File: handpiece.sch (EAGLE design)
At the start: 26 parts, among them IC1 MEGA8-P

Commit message: text marker besides con
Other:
- note added: "To Centerpiece"
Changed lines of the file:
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@@
 <text x="96.52" y="-2.54" size="1.778" layer="97">Only populated on Left-Handpiece</text>
 <text x="5.08" y="-2.54" size="1.778" layer="97">Only populated on Right-Handpiece</text>
+<text x="154.94" y="96.52" size="1.778" layer="97">To Centerpiece</text>
 </plain>
 <instances>

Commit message: proof of concept routing
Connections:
- net D: now also IC1.PB1(OC1A); no longer IC1.PB2(SS/OC1B)
- net EA: now also IC1.PD2(INT0); no longer IC1.PD3(INT1)
- net KR: now also IC1.PD0(RXD); no longer IC1.PD1(TXD)
- net N: now also IC1.PB0(ICP); no longer IC1.PD2(INT0)
- net OU: now also IC1.PD3(INT1); no longer IC1.PD4(XCK/T0)
- net SS: now also IC1.PD1(TXD); no longer IC1.PD0(RXD)
- net Z: now also IC1.PB2(SS/OC1B); no longer IC1.PB1(OC1A)
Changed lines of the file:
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@@
 <setting verticaltext="up"/>
 </settings>
-<grid distance="0.1" unitdist="inch" unit="inch" style="lines" multiple="1" display="yes" altdistance="0.01" altunitdist="inch" altunit="inch"/>
+<grid distance="0.1" unitdist="inch" unit="inch" style="lines" multiple="1" display="no" altdistance="0.01" altunitdist="inch" altunit="inch"/>
 <layers>
 <layer number="1" name="Top" color="4" fill="1" visible="no" active="no"/>
@@
 </segment>
 <segment>
-<pinref part="IC1" gate="G$1" pin="PD0(RXD)"/>
-<wire x1="157.48" y1="10.16" x2="170.18" y2="10.16" width="0.1524" layer="91"/>
+<pinref part="IC1" gate="G$1" pin="PD1(TXD)"/>
+<wire x1="157.48" y1="12.7" x2="170.18" y2="12.7" width="0.1524" layer="91"/>
 </segment>
 </net>
@@
 </segment>
 <segment>
-<pinref part="IC1" gate="G$1" pin="PD1(TXD)"/>
-<wire x1="157.48" y1="12.7" x2="170.18" y2="12.7" width="0.1524" layer="91"/>
+<pinref part="IC1" gate="G$1" pin="PD0(RXD)"/>
+<wire x1="157.48" y1="10.16" x2="170.18" y2="10.16" width="0.1524" layer="91"/>
 </segment>
 </net>
@@
 </segment>
 <segment>
-<pinref part="IC1" gate="G$1" pin="PB1(OC1A)"/>
-<wire x1="157.48" y1="35.56" x2="170.18" y2="35.56" width="0.1524" layer="91"/>
+<pinref part="IC1" gate="G$1" pin="PB2(SS/OC1B)"/>
+<wire x1="157.48" y1="38.1" x2="170.18" y2="38.1" width="0.1524" layer="91"/>
 </segment>
 </net>
@@
 <pinref part="E" gate="G$1" pin="PIN-2"/>
 <wire x1="5.08" y1="-22.86" x2="5.08" y2="-12.7" width="0.1524" layer="91"/>
+<wire x1="5.08" y1="-12.7" x2="53.34" y2="-12.7" width="0.1524" layer="91"/>
+<wire x1="53.34" y1="-12.7" x2="53.34" y2="2.54" width="0.1524" layer="91"/>
 <pinref part="A" gate="G$1" pin="PIN-2"/>
-<wire x1="5.08" y1="-12.7" x2="53.34" y2="-12.7" width="0.1524" layer="91"/>
 <wire x1="53.34" y1="-12.7" x2="99.06" y2="-12.7" width="0.1524" layer="91"/>
 <wire x1="99.06" y1="-12.7" x2="99.06" y2="-22.86" width="0.1524" layer="91"/>
-<wire x1="53.34" y1="-12.7" x2="53.34" y2="2.54" width="0.1524" layer="91"/>
-<junction x="53.34" y="-12.7"/>
+</segment>
+<segment>
+<pinref part="IC1" gate="G$1" pin="PD2(INT0)"/>
+<wire x1="157.48" y1="15.24" x2="170.18" y2="15.24" width="0.1524" layer="91"/>
+</segment>
+</net>
+<net name="OU" class="0">
+<segment>
+<pinref part="U" gate="G$1" pin="PIN-2"/>
+<wire x1="30.48" y1="-22.86" x2="30.48" y2="-15.24" width="0.1524" layer="91"/>
+<wire x1="30.48" y1="-15.24" x2="55.88" y2="-15.24" width="0.1524" layer="91"/>
+<wire x1="55.88" y1="-15.24" x2="121.92" y2="-15.24" width="0.1524" layer="91"/>
+<wire x1="55.88" y1="2.54" x2="55.88" y2="-15.24" width="0.1524" layer="91"/>
+<junction x="55.88" y="-15.24"/>
+<pinref part="O" gate="G$1" pin="PIN-2"/>
+<wire x1="121.92" y1="-15.24" x2="121.92" y2="-22.86" width="0.1524" layer="91"/>
 </segment>
 <segment>
@@
 </segment>
 </net>
-<net name="OU" class="0">
-<segment>
-<pinref part="U" gate="G$1" pin="PIN-2"/>
-<wire x1="30.48" y1="-22.86" x2="30.48" y2="-15.24" width="0.1524" layer="91"/>
-<pinref part="O" gate="G$1" pin="PIN-2"/>
-<wire x1="30.48" y1="-15.24" x2="55.88" y2="-15.24" width="0.1524" layer="91"/>
-<wire x1="55.88" y1="-15.24" x2="121.92" y2="-15.24" width="0.1524" layer="91"/>
-<wire x1="121.92" y1="-15.24" x2="121.92" y2="-22.86" width="0.1524" layer="91"/>
-<wire x1="55.88" y1="2.54" x2="55.88" y2="-15.24" width="0.1524" layer="91"/>
-<junction x="55.88" y="-15.24"/>
-</segment>
-<segment>
-<pinref part="IC1" gate="G$1" pin="PD4(XCK/T0)"/>
-<wire x1="157.48" y1="20.32" x2="170.18" y2="20.32" width="0.1524" layer="91"/>
-</segment>
-</net>
 <net name="D" class="0">
-<segment>
-<pinref part="IC1" gate="G$1" pin="PB2(SS/OC1B)"/>
-<wire x1="157.48" y1="38.1" x2="170.18" y2="38.1" width="0.1524" layer="91"/>
-</segment>
 <segment>
 <pinref part="D" gate="G$1" pin="PIN-2"/>
 <wire x1="114.3" y1="48.26" x2="111.76" y2="48.26" width="0.1524" layer="91"/>
 <wire x1="111.76" y1="2.54" x2="111.76" y2="48.26" width="0.1524" layer="91"/>
+</segment>
+<segment>
+<pinref part="IC1" gate="G$1" pin="PB1(OC1A)"/>
+<wire x1="157.48" y1="35.56" x2="170.18" y2="35.56" width="0.1524" layer="91"/>
 </segment>
 </net>
@@
 </segment>
 <segment>
-<pinref part="IC1" gate="G$1" pin="PD2(INT0)"/>
-<wire x1="157.48" y1="15.24" x2="170.18" y2="15.24" width="0.1524" layer="91"/>
-</segment>
-</net>
+<pinref part="IC1" gate="G$1" pin="PB0(ICP)"/>
+<wire x1="157.48" y1="33.02" x2="170.18" y2="33.02" width="0.1524" layer="91"/>
+</segment>
+</net>

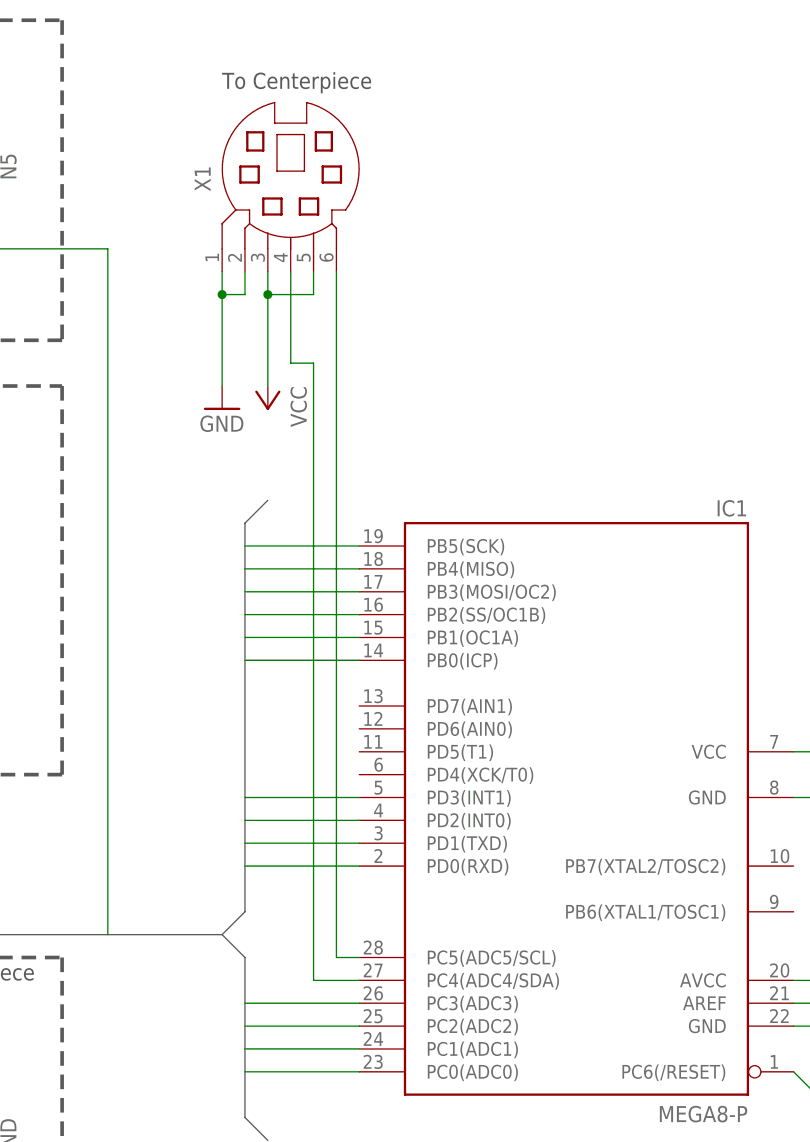
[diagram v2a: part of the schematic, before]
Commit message: add second connector (only one populated on one board)
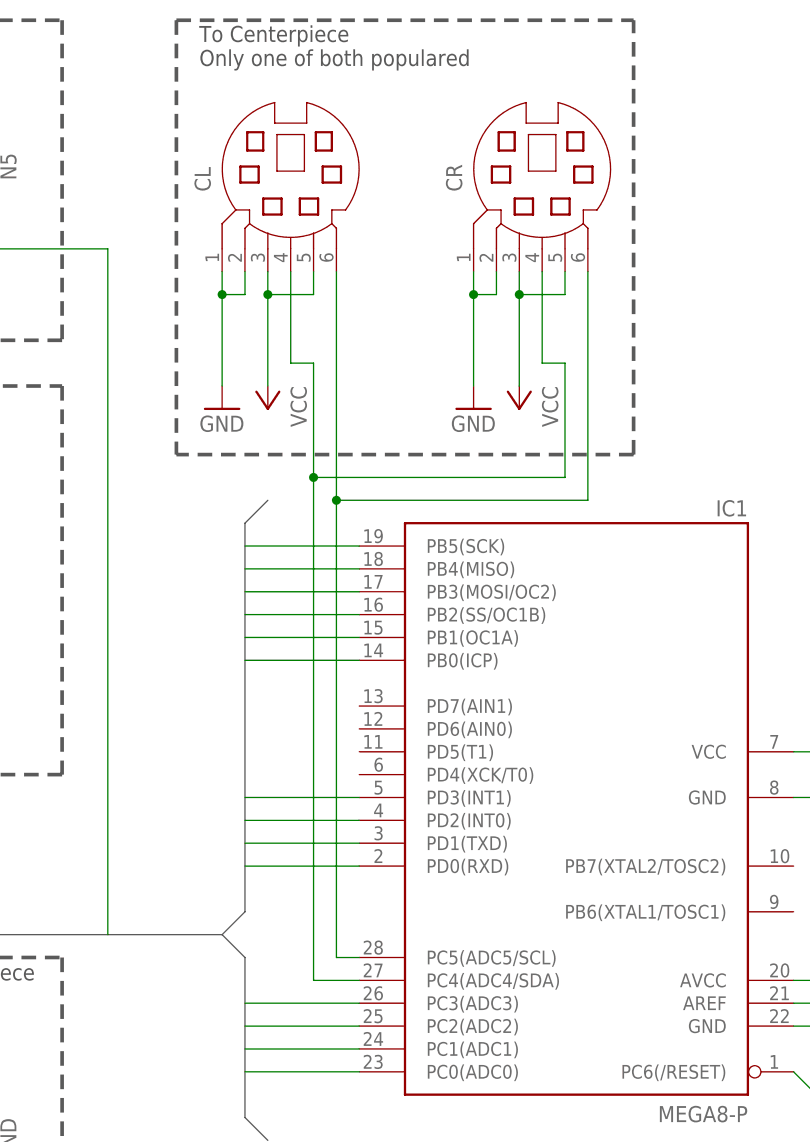
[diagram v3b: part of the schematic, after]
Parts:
- added CR: (no value), con-yamaichi:MD06SS
- renumbered X1 to CL
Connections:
- net GND: now also CR.1, CR.2
- net SCL: now also CR.6
- net SDA: now also CR.4
- net VCC: now also CR.3, CR.5
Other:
- note added: "To Centerpiece Only one of both populared"
- note removed: "To Centerpiece"
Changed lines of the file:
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@@
 <?xml version="1.0" encoding="utf-8"?>
 <!DOCTYPE eagle SYSTEM "eagle.dtd">
-<eagle version="6.4">
+<eagle version="6.5.0">
 <drawing>
 <settings>
@@
 <setting verticaltext="up"/>
 </settings>
-<grid distance="0.1" unitdist="inch" unit="inch" style="lines" multiple="1" display="no" altdistance="0.01" altunitdist="inch" altunit="inch"/>
+<grid distance="0.1" unitdist="inch" unit="inch" style="lines" multiple="1" display="yes" altdistance="0.01" altunitdist="inch" altunit="inch"/>
 <layers>
 <layer number="1" name="Top" color="4" fill="1" visible="no" active="no"/>
@@
 <part name="GND16" library="supply1" deviceset="GND" device=""/>
 <part name="GND17" library="supply1" deviceset="GND" device=""/>
-<part name="X1" library="con-yamaichi" deviceset="MD06SS" device=""/>
+<part name="CL" library="con-yamaichi" deviceset="MD06SS" device=""/>
 <part name="GND18" library="supply1" deviceset="GND" device=""/>
 <part name="P+6" library="supply1" deviceset="VCC" device=""/>
@@
 <part name="GND19" library="supply1" deviceset="GND" device=""/>
 <part name="GND20" library="supply1" deviceset="GND" device=""/>
+<part name="CR" library="con-yamaichi" deviceset="MD06SS" device=""/>
+<part name="GND21" library="supply1" deviceset="GND" device=""/>
+<part name="P+5" library="supply1" deviceset="VCC" device=""/>
 </parts>
 <sheets>
@@
 <text x="96.52" y="-2.54" size="1.778" layer="97">Only populated on Left-Handpiece</text>
 <text x="5.08" y="-2.54" size="1.778" layer="97">Only populated on Right-Handpiece</text>
-<text x="154.94" y="96.52" size="1.778" layer="97">To Centerpiece</text>
+<text x="152.4" y="99.06" size="1.778" layer="97">To Centerpiece
+Only one of both populared</text>
+<wire x1="149.86" y1="104.14" x2="200.66" y2="104.14" width="0.4064" layer="97" style="shortdash"/>
+<wire x1="200.66" y1="55.88" x2="200.66" y2="104.14" width="0.4064" layer="97" style="shortdash"/>
+<wire x1="200.66" y1="55.88" x2="149.86" y2="55.88" width="0.4064" layer="97" style="shortdash"/>
+<wire x1="149.86" y1="104.14" x2="149.86" y2="55.88" width="0.4064" layer="97" style="shortdash"/>
 </plain>
 <instances>
@@
 <instance part="GND16" gate="1" x="91.44" y="38.1" rot="R180"/>
 <instance part="GND17" gate="1" x="114.3" y="38.1" rot="R180"/>
-<instance part="X1" gate="G$1" x="162.56" y="86.36" rot="R90"/>
+<instance part="CL" gate="G$1" x="162.56" y="86.36" rot="R90"/>
 <instance part="GND18" gate="1" x="154.94" y="60.96"/>
 <instance part="P+6" gate="VCC" x="160.02" y="60.96" rot="R180"/>
@@
 <instance part="GND19" gate="1" x="106.68" y="-20.32" rot="R90"/>
 <instance part="GND20" gate="1" x="129.54" y="-20.32" rot="R90"/>
+<instance part="CR" gate="G$1" x="190.5" y="86.36" rot="R90"/>
+<instance part="GND21" gate="1" x="182.88" y="60.96"/>
+<instance part="P+5" gate="VCC" x="187.96" y="60.96" rot="R180"/>
 </instances>
 <busses>
@@
 <segment>
 <pinref part="GND18" gate="1" pin="GND"/>
-<pinref part="X1" gate="G$1" pin="1"/>
+<pinref part="CL" gate="G$1" pin="1"/>
 <wire x1="154.94" y1="63.5" x2="154.94" y2="73.66" width="0.1524" layer="91"/>
-<pinref part="X1" gate="G$1" pin="2"/>
+<pinref part="CL" gate="G$1" pin="2"/>
 <wire x1="154.94" y1="73.66" x2="154.94" y2="76.2" width="0.1524" layer="91"/>
 <wire x1="157.48" y1="76.2" x2="157.48" y2="73.66" width="0.1524" layer="91"/>
@@
 <wire x1="127" y1="-22.86" x2="127" y2="-20.32" width="0.1524" layer="91"/>
 </segment>
+<segment>
+<pinref part="GND21" gate="1" pin="GND"/>
+<pinref part="CR" gate="G$1" pin="1"/>
+<wire x1="182.88" y1="63.5" x2="182.88" y2="73.66" width="0.1524" layer="91"/>
+<pinref part="CR" gate="G$1" pin="2"/>
+<wire x1="182.88" y1="73.66" x2="182.88" y2="76.2" width="0.1524" layer="91"/>
+<wire x1="182.88" y1="73.66" x2="185.42" y2="73.66" width="0.1524" layer="91"/>
+<wire x1="185.42" y1="73.66" x2="185.42" y2="76.2" width="0.1524" layer="91"/>
+<junction x="182.88" y="73.66"/>
+</segment>
 </net>
 <net name="VCC" class="0">
@@
 </segment>
 <segment>
-<pinref part="X1" gate="G$1" pin="3"/>
+<pinref part="CL" gate="G$1" pin="3"/>
 <pinref part="P+6" gate="VCC" pin="VCC"/>
 <wire x1="160.02" y1="76.2" x2="160.02" y2="73.66" width="0.1524" layer="91"/>
-<pinref part="X1" gate="G$1" pin="5"/>
+<pinref part="CL" gate="G$1" pin="5"/>
 <wire x1="160.02" y1="73.66" x2="160.02" y2="63.5" width="0.1524" layer="91"/>
 <wire x1="165.1" y1="76.2" x2="165.1" y2="73.66" width="0.1524" layer="91"/>
 <wire x1="165.1" y1="73.66" x2="160.02" y2="73.66" width="0.1524" layer="91"/>
 <junction x="160.02" y="73.66"/>
+</segment>
+<segment>
+<pinref part="P+5" gate="VCC" pin="VCC"/>
+<pinref part="CR" gate="G$1" pin="3"/>
+<wire x1="187.96" y1="63.5" x2="187.96" y2="73.66" width="0.1524" layer="91"/>
+<pinref part="CR" gate="G$1" pin="5"/>
+<wire x1="187.96" y1="73.66" x2="187.96" y2="76.2" width="0.1524" layer="91"/>
+<wire x1="187.96" y1="73.66" x2="193.04" y2="73.66" width="0.1524" layer="91"/>
+<wire x1="193.04" y1="73.66" x2="193.04" y2="76.2" width="0.1524" layer="91"/>
+<junction x="187.96" y="73.66"/>
 </segment>
 </net>
@@
 <pinref part="IC1" gate="G$1" pin="PC5(ADC5/SCL)"/>
 <wire x1="170.18" y1="0" x2="167.64" y2="0" width="0.1524" layer="91"/>
-<wire x1="167.64" y1="0" x2="167.64" y2="76.2" width="0.1524" layer="91"/>
-<pinref part="X1" gate="G$1" pin="6"/>
+<wire x1="167.64" y1="0" x2="167.64" y2="50.8" width="0.1524" layer="91"/>
+<pinref part="CL" gate="G$1" pin="6"/>
+<pinref part="CR" gate="G$1" pin="6"/>
+<wire x1="167.64" y1="50.8" x2="167.64" y2="76.2" width="0.1524" layer="91"/>
+<wire x1="195.58" y1="76.2" x2="195.58" y2="50.8" width="0.1524" layer="91"/>
+<wire x1="195.58" y1="50.8" x2="167.64" y2="50.8" width="0.1524" layer="91"/>
+<junction x="167.64" y="50.8"/>
 </segment>
 </net>
@@
 <pinref part="IC1" gate="G$1" pin="PC4(ADC4/SDA)"/>
 <wire x1="170.18" y1="-2.54" x2="165.1" y2="-2.54" width="0.1524" layer="91"/>
-<wire x1="165.1" y1="-2.54" x2="165.1" y2="66.04" width="0.1524" layer="91"/>
-<pinref part="X1" gate="G$1" pin="4"/>
+<wire x1="165.1" y1="-2.54" x2="165.1" y2="53.34" width="0.1524" layer="91"/>
+<pinref part="CL" gate="G$1" pin="4"/>
+<wire x1="165.1" y1="53.34" x2="165.1" y2="66.04" width="0.1524" layer="91"/>
 <wire x1="162.56" y1="76.2" x2="162.56" y2="66.04" width="0.1524" layer="91"/>
 <wire x1="165.1" y1="66.04" x2="162.56" y2="66.04" width="0.1524" layer="91"/>
-</segment>
-</net>
+<pinref part="CR" gate="G$1" pin="4"/>
+<wire x1="190.5" y1="76.2" x2="190.5" y2="66.04" width="0.1524" layer="91"/>
+<wire x1="190.5" y1="66.04" x2="193.04" y2="66.04" width="0.1524" layer="91"/>
+<wire x1="193.04" y1="66.04" x2="193.04" y2="53.34" width="0.1524" layer="91"/>
+<wire x1="193.04" y1="53.34" x2="165.1" y2="53.34" width="0.1524" layer="91"/>
+<junction x="165.1" y="53.34"/>
+</segment>
+</net>

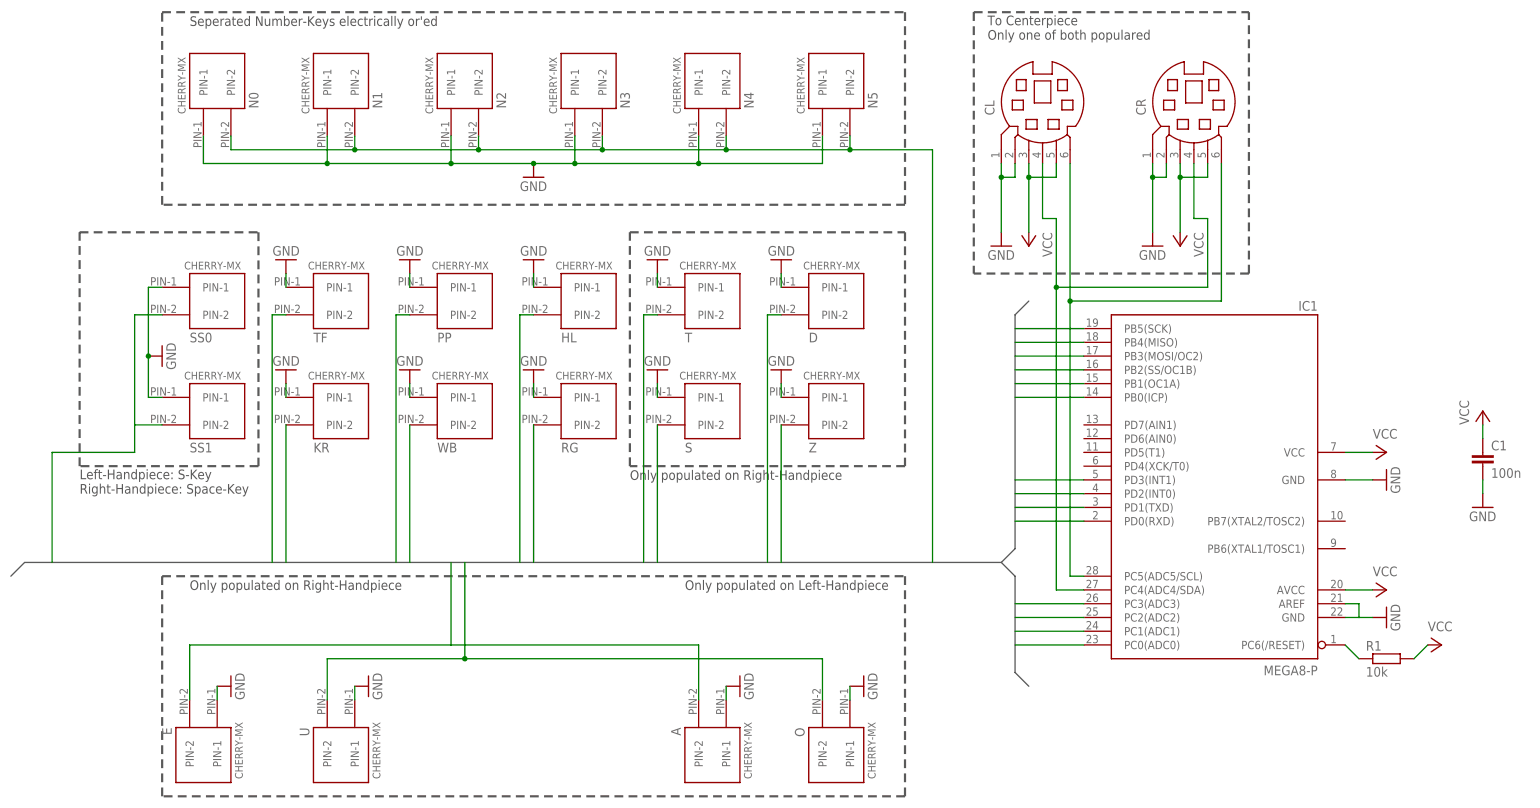
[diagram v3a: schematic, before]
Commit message: wire i²c
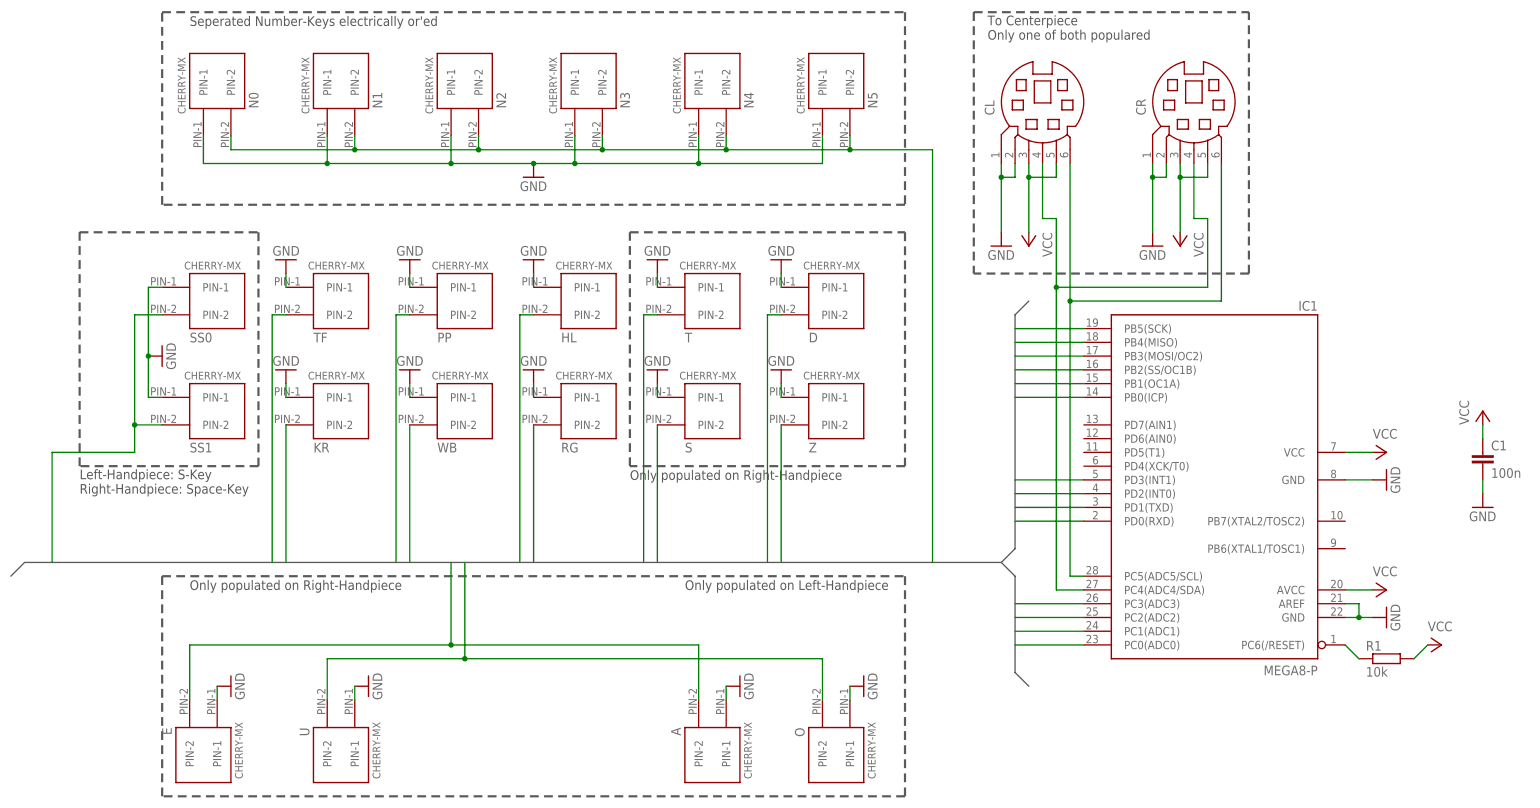
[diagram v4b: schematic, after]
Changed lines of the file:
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@@
 <pinref part="IC1" gate="G$1" pin="GND"/>
 <wire x1="220.98" y1="-7.62" x2="218.44" y2="-7.62" width="0.1524" layer="91"/>
+<junction x="220.98" y="-7.62"/>
 </segment>
 <segment>
@@
 <wire x1="-5.08" y1="22.86" x2="-20.32" y2="22.86" width="0.1524" layer="91"/>
 <wire x1="-20.32" y1="22.86" x2="-20.32" y2="2.54" width="0.1524" layer="91"/>
+<junction x="-5.08" y="27.94"/>
 </segment>
 <segment>
@@
 <wire x1="53.34" y1="-12.7" x2="99.06" y2="-12.7" width="0.1524" layer="91"/>
 <wire x1="99.06" y1="-12.7" x2="99.06" y2="-22.86" width="0.1524" layer="91"/>
-</segment>
-<segment>
+<junction x="53.34" y="-12.7"/>
+</segment>
+<segment>
